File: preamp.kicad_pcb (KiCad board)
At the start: 2 copper layers, 44 parts, among them P1 CONN_01X04, P2 CONN_01X02, P3 CONN_01X04, T1 TRANSFO2, U1 OPA137N, U2 LM7815CT, U3 LM7915CT, U4 OPA137N

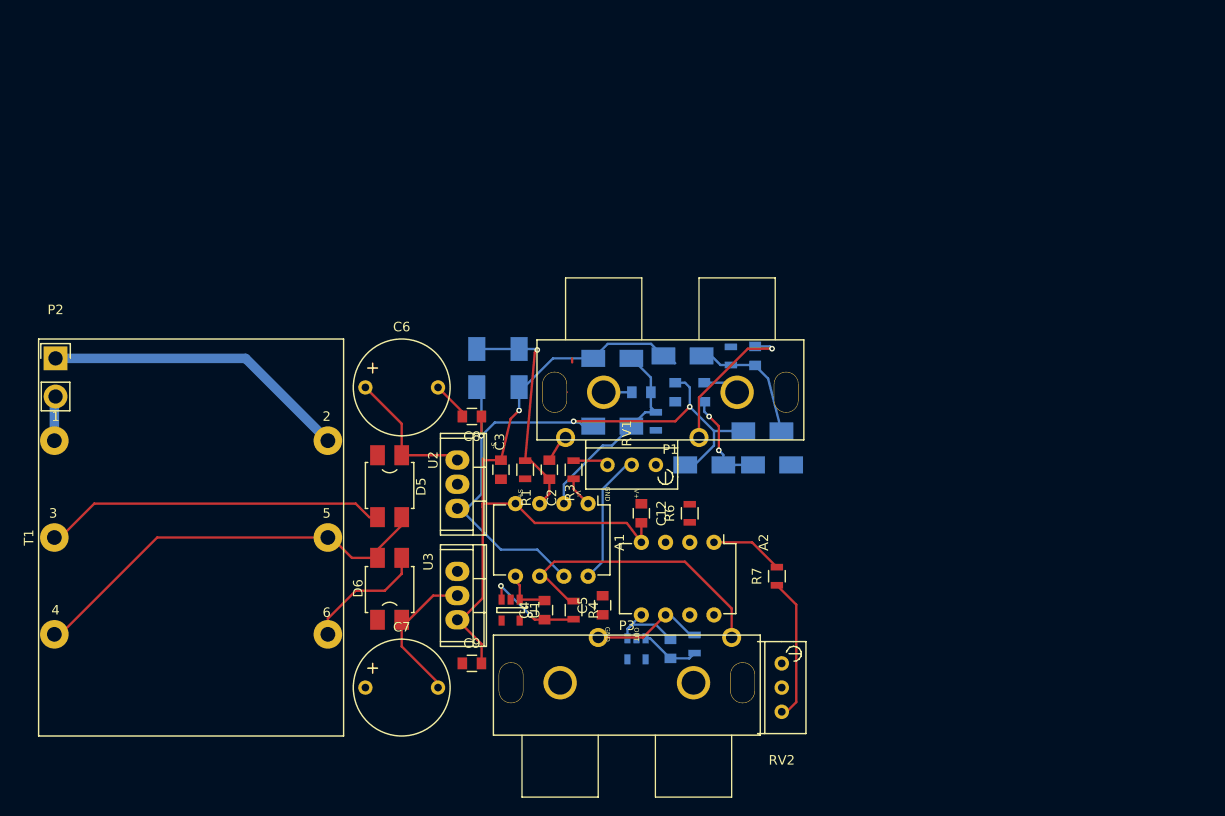
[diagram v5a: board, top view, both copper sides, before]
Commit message: Finish adding PSU and second channel.  Ready for fab?
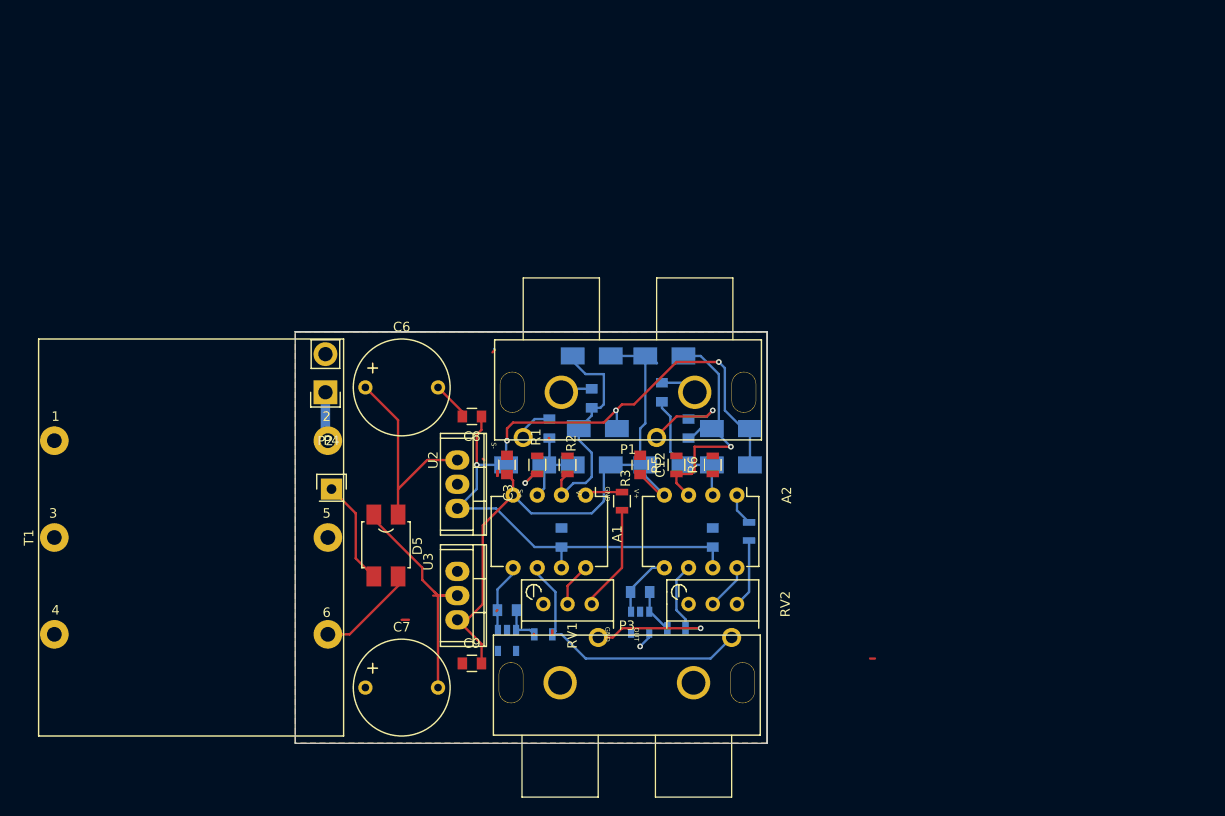
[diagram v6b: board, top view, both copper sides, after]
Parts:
- removed D6: Diode_Bridge, preamp:Bridge-Rectifier-SOIC-4
- added P4: CONN_01X01, Pin_Headers:Pin_Header_Straight_1x01, F.Cu at (71.1, 73.7)
- C2, C4, C5, R4, R7, U1: moved to B.Cu
- R2, R5: moved to F.Cu
- moved P2 28.5 mm to (70.5, 63.5), turned to 180 degrees
- moved RV1 18.8 mm to (93.3, 85.7), turned to 270 degrees
- moved C14 15.7 mm to (111.1, 78.7), turned to 270 degrees
- moved R5 12.8 mm to (107.3, 71.1)
- moved D2 12.7 mm to (98.4, 71.1), turned to 0 degrees
- moved RV2 11.6 mm to (108.6, 85.7), turned to 270 degrees
- moved D1 11.4 mm to (91.4, 71.1), turned to 0 degrees
- moved D10 11.3 mm to (106.0, 71.1), turned to 180 degrees
- moved C11 10.3 mm to (108.6, 67.3)
- moved R2 10.3 mm to (95.9, 71.1), turned to 90 degrees
- moved C5 8.32 mm to (95.2, 78.7), turned to 270 degrees
- moved C13 6.76 mm to (103.5, 84.5), turned to 180 degrees
- moved D5 6.23 mm to (76.8, 79.4)
- moved R3 6.06 mm to (101.6, 74.9), turned to 90 degrees
- moved R6 5.62 mm to (111.1, 71.1)
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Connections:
- D5 pad 1: GND -> Net-(C7-Pad2)
- RV1 pad 1: Net-(RV1-Pad1) -> (no net)
- RV2 pad 1: Net-(RV2-Pad1) -> (no net)
- T1 pad 4: Net-(D5-Pad2) -> GND
- T1 pad 5: Net-(D5-Pad2) -> GND
- T1 pad 6: Net-(D6-Pad4) -> Net-(D5-Pad2)
- U1 pad 2: Net-(U1-Pad2) -> (no net)
- U1 pad 5: Net-(U1-Pad5) -> (no net)
- U4 pad 2: Net-(U4-Pad2) -> (no net)
- U4 pad 5: Net-(U4-Pad5) -> (no net)
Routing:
- net Net-(D5-Pad2): track 44.3 -> 11.3 mm
- net Earth: track 32.7 -> 5.69 mm
- net Net-(D5-Pad4): track 36.0 -> 11.6 mm
- net +15V: track 73.3 -> 92.0 mm, vias 3 -> 4
- net Net-(A2-Pad3): track 13.6 -> 28.5 mm, vias 0 -> 1
- net Net-(D6-Pad4): track 13.0 -> 0.00 mm
- net Net-(C7-Pad2): track 15.6 -> 26.1 mm
- net Net-(A1-Pad3): track 24.6 -> 14.6 mm
- net Net-(A1-Pad8): track 13.9 -> 4.60 mm
- net Net-(A2-Pad6): track 12.0 -> 20.5 mm, vias 0 -> 1
- net Net-(C6-Pad1): track 14.7 -> 23.0 mm
- net Net-(R7-Pad1): track 15.0 -> 7.20 mm
- net Net-(R3-Pad1): track 3.74 -> 11.2 mm
- net -15V: track 75.0 -> 68.2 mm, vias 1 -> 0
- net Net-(C4-Pad1): track 11.0 -> 4.20 mm, vias 2 -> 0
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- added copper zone on B.Cu, net GND
- added copper zone on F.Cu, net GND
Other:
- board outline added: 49.5 x 43.2 mm

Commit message: Cleanup a label I missed
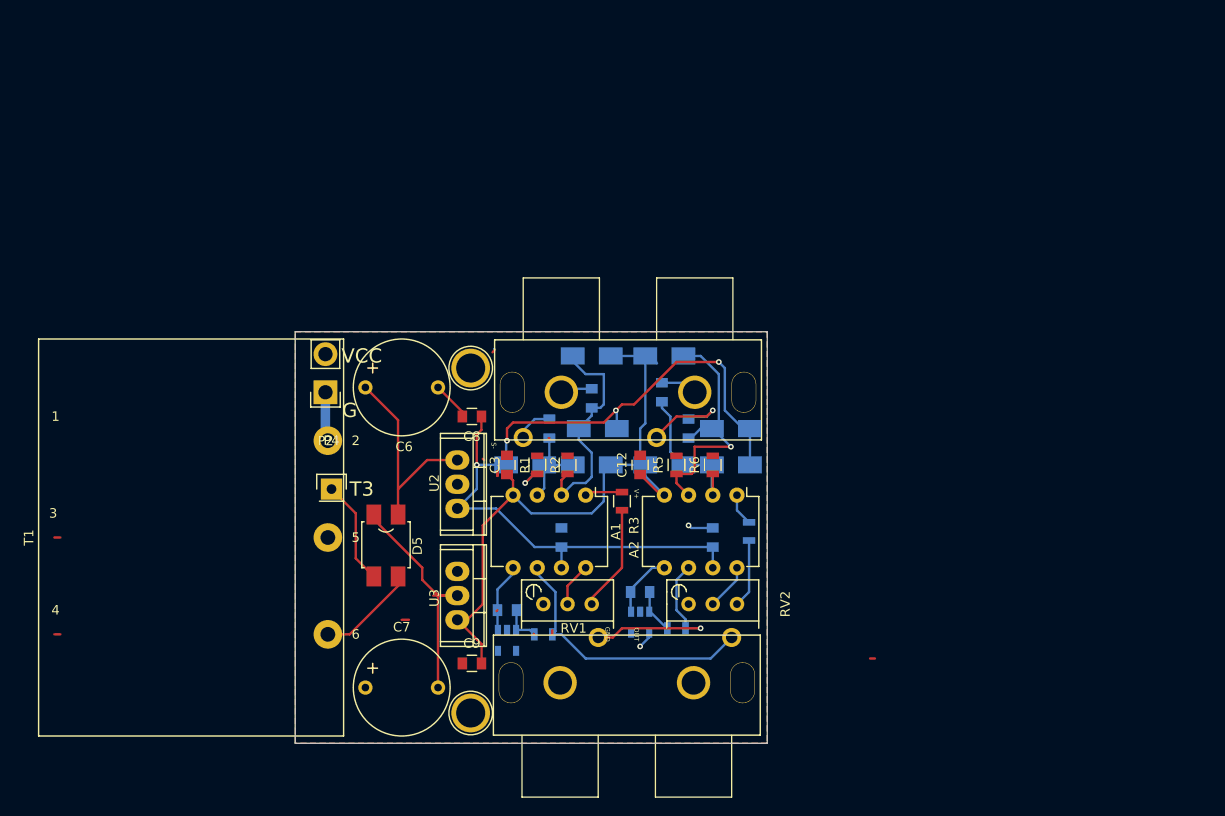
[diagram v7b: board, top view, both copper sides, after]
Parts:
- added REF**: 1pin, Connect:1pin, F.Cu at (85.7, 97.2)
- added REF**: 1pin, Connect:1pin, F.Cu at (85.7, 61.0)
- T1: footprint preamp:preamp_transformer_6pin -> preamp:preamp_transformer_6pin_half
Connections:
- P2 pad 2: VCC -> (no net)
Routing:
- net Net-(A2-Pad2): track 13.8 -> 16.0 mm
- net GND: track 6.64 -> 8.66 mm, vias 1 -> 2
- net (no net): track 3.75 -> 5.02 mm
- net Net-(D5-Pad4): track 11.6 -> 11.0 mm
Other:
- board text added: "G"
- board text added: "T3"
- board text added: "VCC"
- board text removed: "S+"
- board text removed: "V-"

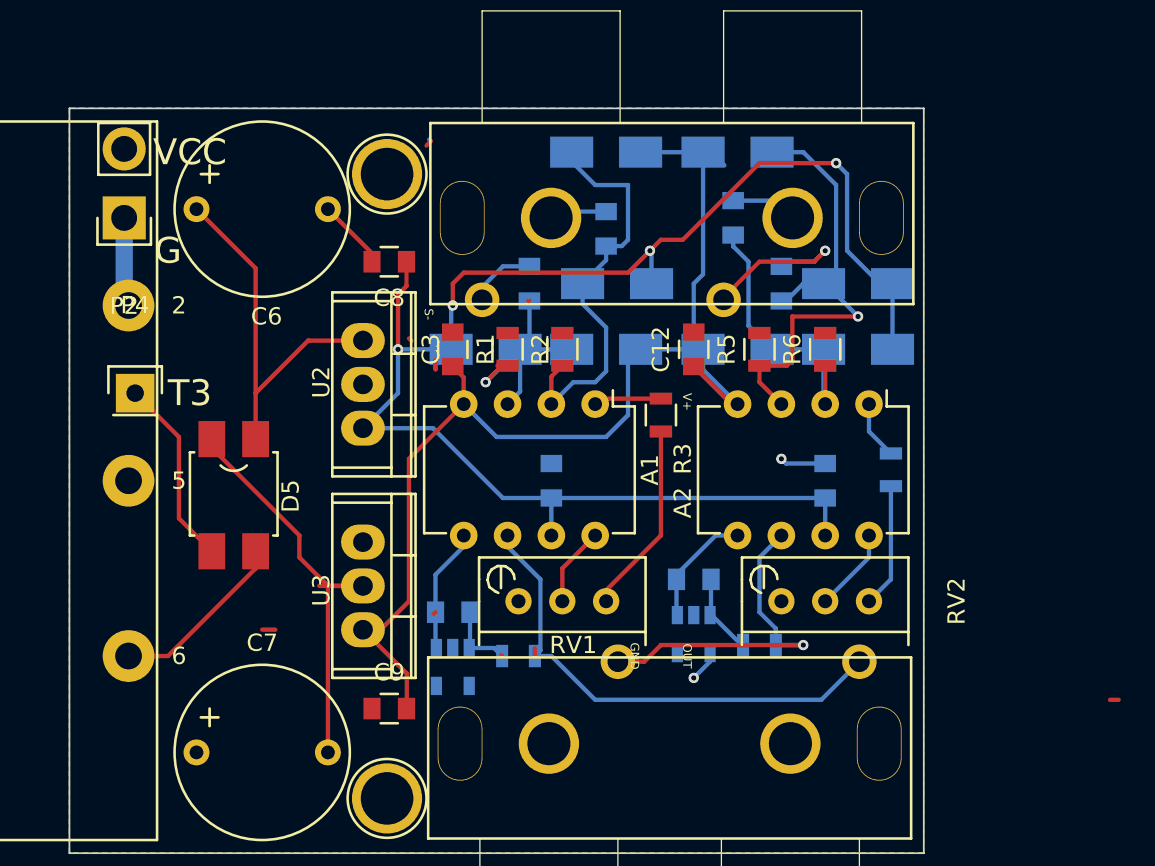
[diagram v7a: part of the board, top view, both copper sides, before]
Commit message: Add power cable items to BOM and misc layout cleanup.
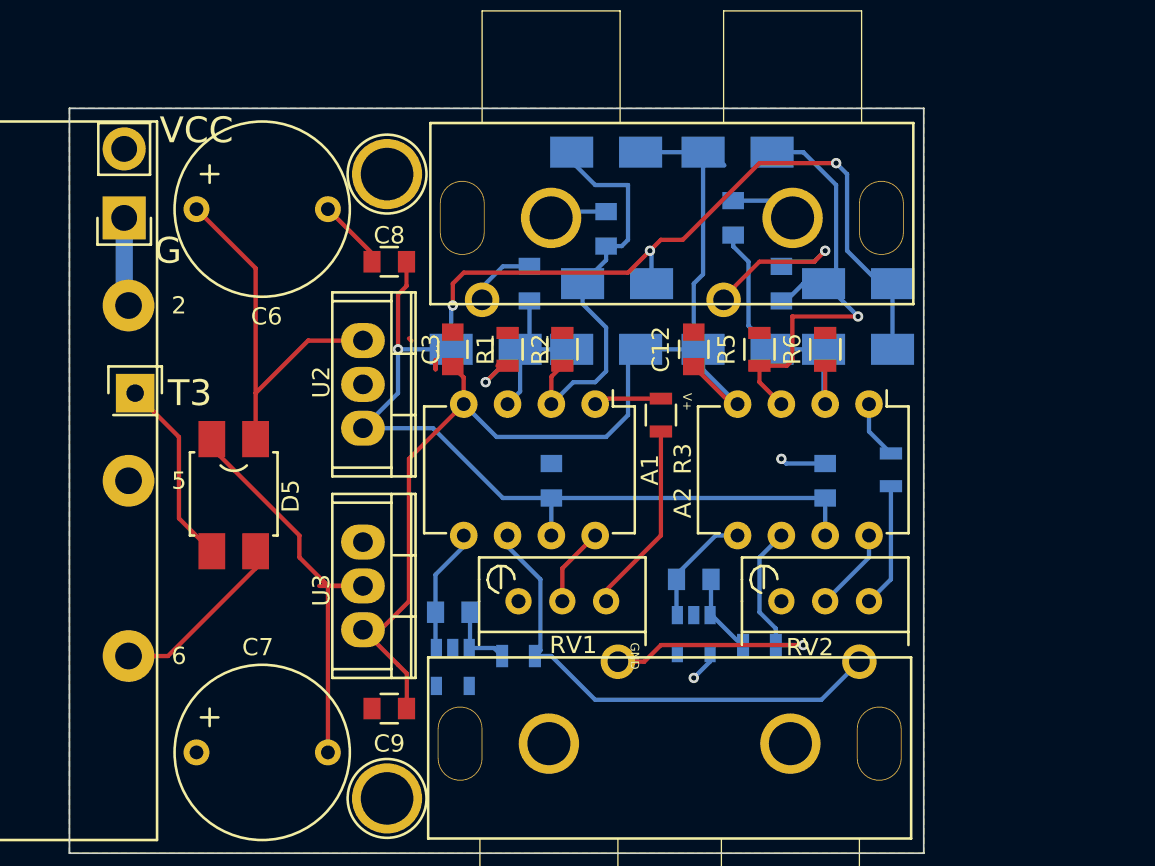
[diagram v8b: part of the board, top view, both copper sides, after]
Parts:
- C6, C7: footprint Capacitors_Elko_ThroughHole:Elko_vert_20x10mm_RM7.5 -> preamp:preamp_Elko_vert_20x10mm_RM7.5
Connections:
- P2 pad 2: (no net) -> VCC
- RV1 pad 1: (no net) -> Net-(RV1-Pad1)
- RV2 pad 1: (no net) -> Net-(RV2-Pad1)
- U1 pad 2: (no net) -> Net-(U1-Pad2)
- U1 pad 5: (no net) -> Net-(U1-Pad5)
- U4 pad 2: (no net) -> Net-(U4-Pad2)
- U4 pad 5: (no net) -> Net-(U4-Pad5)
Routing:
- net (no net): track 5.02 -> 2.52 mm
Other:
- board text removed: "OUT"
- board text removed: "S-"
